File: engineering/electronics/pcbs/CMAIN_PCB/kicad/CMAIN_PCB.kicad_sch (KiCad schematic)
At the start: 79 parts, among them IC1 TSYS01, J1 RPI_5_WITH_SSQ-120-01-F-D, J10 1778719, J11 M9N-G4-3100, J12 B04B-JWPF-SK-R, J13 B04B-JWPF-SK-R, J14 XT30PW-F, J15 SM04B-GHS-TB_LF__SN_, J16 1778719, J17 SM03B-GHS-TB(LF)(SN), J19 1778719, J2 1778719, J21 1778719, J23 B04B-JWPF-SK-R, J24 1778719, J27 B04B-JWPF-SK-R, J29 B06B-JWPF-SK-R, J3 AXK6S00547YG, J30 B06B-JWPF-SK-R, J31 B06B-JWPF-SK-R, J32 B04B-JWPF-SK-R, J35 SM04B-GHS-TB_LF__SN_, J36 SM05B-GHS-TB_LF__SN_, J37 B04B-JWPF-SK-R, J38 B04B-JWPF-SK-R, J39 B04B-JWPF-SK-R, J4 AXK6S00547YG, J40 B04B-JWPF-SK-R, J41 SM06B-GHS-TB_LF__SN_, J43 B04B-JWPF-SK-R, J45 B04B-JWPF-SK-R, J46 B04B-JWPF-SK-R, J48 B04B-JWPF-SK-R, J49 B04B-JWPF-SK-R, J5 SM04B-GHS-TB_LF__SN_, J50 1778719, J52 B04B-JWPF-SK-R, J53 B04B-JWPF-SK-R, J55 B04B-JWPF-SK-R, J56 B04B-JWPF-SK-R, J57 B04B-JWPF-SK-R, J6 1778719, J7 SM04B-GHS-TB_LF__SN_, J8 B04B-JWPF-SK-R, J9 SM04B-GHS-TB_LF__SN_, U10 SMTSO25100CTJ, U11 SMTSO25100CTJ, U12 SMTSO25100CTJ, U3 SMTSOM380BTR, U6 SMTSOM380BTR, U7 SMTSOM380BTR, U8 SMTSOM380BTR, U9 SMTSO25100CTJ

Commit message: Resolve CMAIN ERC warnings
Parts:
- CN18, CN20, CN22, CN54: symbol EasyEDA_Lib_CMAIN:BM04B-GHS-TBT(LF)(SN) -> CMAIN_PCB:BM04B-GHS-TBT(LF)(SN)
- D5: symbol EasyEDA_Lib_CMAIN:USBLC6-2SC6 -> CMAIN_PCB:USBLC6-2SC6
- D8: symbol EasyEDA_Lib_CMAIN:SS14_C7420316 -> CMAIN_PCB:SS14_C7420316
- U19, U20, U21, U5: symbol EasyEDA_Lib_CMAIN:SMTSO3050CTJ -> CMAIN_PCB:SMTSO3050CTJ
- USB33: symbol EasyEDA_Lib_CMAIN:TYPEC-303-ACP16 -> CMAIN_PCB:TYPEC-303-ACP16
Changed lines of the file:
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@@
 	)
 	(symbol
-		(lib_id "EasyEDA_Lib_CMAIN:SMTSO3050CTJ")
+		(lib_id "CMAIN_PCB:SMTSO3050CTJ")
 		(at 137.16 216.662 0)
 		(unit 1)
@@
 	)
 	(symbol
-		(lib_id "EasyEDA_Lib_CMAIN:USBLC6-2SC6")
+		(lib_id "CMAIN_PCB:USBLC6-2SC6")
 		(at 485.648 325.628 0)
 		(unit 1)
@@
 	)
 	(symbol
-		(lib_id "EasyEDA_Lib_CMAIN:BM04B-GHS-TBT(LF)(SN)")
+		(lib_id "CMAIN_PCB:BM04B-GHS-TBT(LF)(SN)")
 		(at 285.75 151.13 0)
 		(unit 1)
@@
 	)
 	(symbol
-		(lib_id "EasyEDA_Lib_CMAIN:BM04B-GHS-TBT(LF)(SN)")
+		(lib_id "CMAIN_PCB:BM04B-GHS-TBT(LF)(SN)")
 		(at 265.43 158.75 0)
 		(unit 1)
@@
 	)
 	(symbol
-		(lib_id "EasyEDA_Lib_CMAIN:SMTSO3050CTJ")
+		(lib_id "CMAIN_PCB:SMTSO3050CTJ")
 		(at 137.16 233.172 0)
 		(unit 1)
@@
 	)
 	(symbol
-		(lib_id "EasyEDA_Lib_CMAIN:TYPEC-303-ACP16")
+		(lib_id "CMAIN_PCB:TYPEC-303-ACP16")
 		(at 425.958 325.628 180)
 		(unit 1)
@@
 	)
 	(symbol
-		(lib_id "EasyEDA_Lib_CMAIN:BM04B-GHS-TBT(LF)(SN)")
+		(lib_id "CMAIN_PCB:BM04B-GHS-TBT(LF)(SN)")
 		(at 306.07 156.21 0)
 		(unit 1)
@@
 	)
 	(symbol
-		(lib_id "EasyEDA_Lib_CMAIN:BM04B-GHS-TBT(LF)(SN)")
+		(lib_id "CMAIN_PCB:BM04B-GHS-TBT(LF)(SN)")
 		(at 242.57 153.67 0)
 		(unit 1)
@@
 	)
 	(symbol
-		(lib_id "EasyEDA_Lib_CMAIN:SS14_C7420316")
+		(lib_id "CMAIN_PCB:SS14_C7420316")
 		(at 453.898 309.118 0)
 		(unit 1)
@@
 	)
 	(symbol
-		(lib_id "EasyEDA_Lib_CMAIN:SMTSO3050CTJ")
+		(lib_id "CMAIN_PCB:SMTSO3050CTJ")
 		(at 137.16 222.25 0)
 		(unit 1)
@@
 	)
 	(symbol
-		(lib_id "EasyEDA_Lib_CMAIN:SMTSO3050CTJ")
+		(lib_id "CMAIN_PCB:SMTSO3050CTJ")
 		(at 137.16 227.584 0)
 		(unit 1)

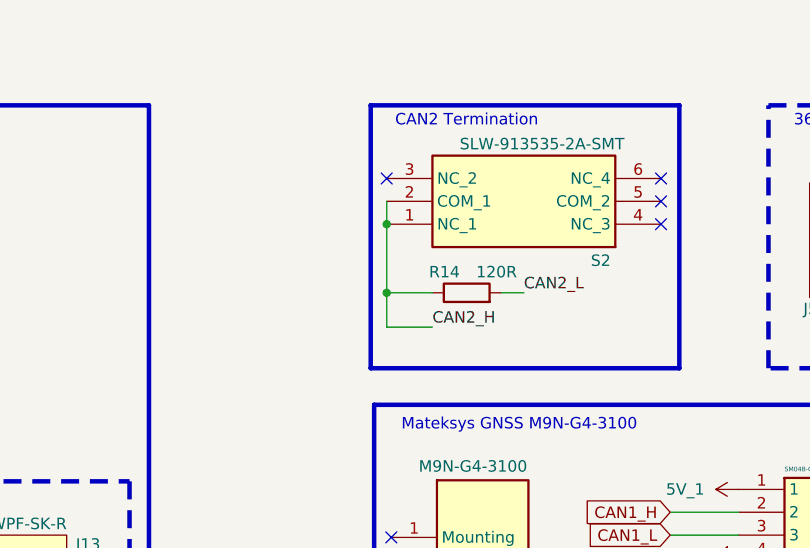
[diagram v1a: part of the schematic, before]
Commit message: Update CMAIN PCB routing from latest archive
Import Julius's latest CMAIN KiCad update, excluding local .history and backup archives. Remap undefined Rescue footprint graphics to F.Fab so KiCad CLI can load the board, and add KiCad ERC/DRC reports.
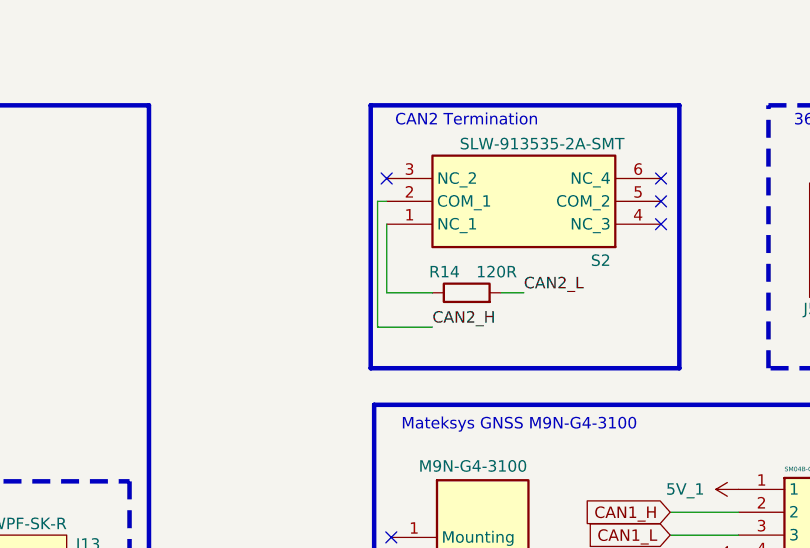
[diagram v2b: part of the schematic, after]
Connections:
- net CAN2_H: no longer R14.1, S2.1 (NC_1)
- new net: R14.1, S2.1 (NC_1)
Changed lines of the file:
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@@
-	)
-	(junction
-		(at 407.416 46.228)
-		(diameter 0)
-		(color 0 0 0 0)
 	)
 	(junction
@@
 	)
 	(junction
-		(at 407.416 38.608)
-		(diameter 0)
-		(color 0 0 0 0)
-	)
-	(junction
 		(at 106.426 223.012)
 		(diameter 0)
@@
 	(wire
 		(pts
+			(xy 406.4 36.068) (xy 407.416 36.068)
+		)
+		(stroke
+			(width 0)
+			(type default)
+		)
+	)
+	(wire
+		(pts
 			(xy 255.143 321.818) (xy 255.143 316.738)
 		)
@@
 	(wire
 		(pts
+			(xy 407.416 38.608) (xy 407.416 46.228)
+		)
+		(stroke
+			(width 0)
+			(type default)
+		)
+	)
+	(wire
+		(pts
 			(xy 255.016 286.004) (xy 261.366 286.004)
 		)
@@
 	(wire
 		(pts
+			(xy 406.4 50.038) (xy 412.496 50.038)
+		)
+		(stroke
+			(width 0)
+			(type default)
+		)
+	)
+	(wire
+		(pts
 			(xy 433.578 314.198) (xy 441.96 314.198)
 		)
@@
 	(wire
 		(pts
+			(xy 406.4 50.038) (xy 406.4 36.068)
+		)
+		(stroke
+			(width 0)
+			(type default)
+		)
+	)
+	(wire
+		(pts
 			(xy 460.248 318.008) (xy 469.138 318.008)
 		)
@@
 	(wire
 		(pts
-			(xy 407.416 50.038) (xy 412.496 50.038)
-		)
-		(stroke
-			(width 0)
-			(type default)
-		)
-	)
-	(wire
-		(pts
 			(xy 424.18 171.196) (xy 426.72 171.196)
 		)
@@
 	(wire
 		(pts
-			(xy 407.416 36.068) (xy 407.416 38.608)
-		)
-		(stroke
-			(width 0)
-			(type default)
-		)
-	)
-	(wire
-		(pts
 			(xy 327.914 113.538) (xy 335.534 113.538)
 		)
@@
 	(wire
 		(pts
-			(xy 407.416 46.228) (xy 407.416 50.038)
-		)
-		(stroke
-			(width 0)
-			(type default)
-		)
-	)
-	(wire
-		(pts
 			(xy 359.156 80.772) (xy 359.156 83.312)
 		)
@@
 		)
 		(stroke
-			(width 0)
-			(type default)
-		)
-	)
-	(wire
-		(pts
-			(xy 407.416 38.608) (xy 407.416 46.228)
-		)
-		(stroke

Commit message: Clean up CMAIN part value fields
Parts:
- C1: value 100nF -> 100nF 50V; footprint CMAIN_PCB:fp_71505040a9 -> Capacitor_SMD:C_0805_2012Metric_Pad1.18x1.45mm_HandSolder
- CN18, CN20, CN22, CN54: value (none) -> BM04B-GHS-TBT(LF)(SN)
- D5: value (none) -> USBLC6-2SC6
- D8: value (none) -> SS14
- J11: now not fitted
- R10, R11: value 10k -> 10k 150V; footprint CMAIN_PCB:fp_9fb50b8536 -> Resistor_SMD:R_0805_2012Metric_Pad1.20x1.40mm_HandSolder
- R12, R13: value 5K1 -> 5K1 150V; footprint CMAIN_PCB:fp_9fb50b8536 -> Resistor_SMD:R_0805_2012Metric_Pad1.20x1.40mm_HandSolder
- R14: value 120R -> 120R 150V; footprint CMAIN_PCB:fp_9fb50b8536 -> Resistor_SMD:R_0805_2012Metric_Pad1.20x1.40mm_HandSolder
- R2, R4, R5, R8: value 100k -> 100k 150V; footprint CMAIN_PCB:fp_9fb50b8536 -> Resistor_SMD:R_0805_2012Metric_Pad1.20x1.40mm_HandSolder
- U19, U20, U21, U5: value (none) -> SMTSO3050CTJ
- USB33: value (none) -> TYPEC-303-ACP16
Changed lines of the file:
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@@
 			)
 		)
-		(property "Value" ""
+		(property "Value" "SMTSO3050CTJ"
 			(at 137.16 216.662 0)
 			(show_name no)
@@
 			)
 		)
-		(property "Value" "100nF"
+		(property "Value" "100nF 50V"
 			(at 448.31 136.906 0)
 			(show_name no)
@@
 			)
 		)
-		(property "Footprint" "CMAIN_PCB:fp_71505040a9"
+		(property "Footprint" "Capacitor_SMD:C_0805_2012Metric_Pad1.18x1.45mm_HandSolder"
 			(at 448.31 143.256 0)
 			(hide yes)
@@
 			)
 		)
-		(property "Value" "120R"
+		(property "Value" "120R 150V"
 			(at 421.894 43.18 90)
 			(show_name no)
@@
 			)
 		)
-		(property "Footprint" "CMAIN_PCB:fp_9fb50b8536"
+		(property "Footprint" "Resistor_SMD:R_0805_2012Metric_Pad1.20x1.40mm_HandSolder"
 			(at 416.306 47.498 90)
 			(hide yes)
@@
 			)
 		)
-		(property "Value" ""
+		(property "Value" "USBLC6-2SC6"
 			(at 485.648 325.628 0)
 			(show_name no)
@@
 			)
 		)
-		(property "Value" ""
+		(property "Value" "BM04B-GHS-TBT(LF)(SN)"
 			(at 285.75 151.13 0)
 			(show_name no)
@@
 			)
 		)
-		(property "Value" "10k"
+		(property "Value" "10k 150V"
 			(at 429.26 171.196 90)
 			(show_name no)
@@
 			)
 		)
-		(property "Footprint" "CMAIN_PCB:fp_9fb50b8536"
+		(property "Footprint" "Resistor_SMD:R_0805_2012Metric_Pad1.20x1.40mm_HandSolder"
 			(at 430.53 169.926 90)
 			(hide yes)
@@
 			)
 		)
-		(property "Value" ""
+		(property "Value" "BM04B-GHS-TBT(LF)(SN)"
 			(at 265.43 158.75 0)
 			(show_name no)
@@
 		(on_board yes)
 		(in_pos_files yes)
-		(dnp no)
+		(dnp yes)
 		(property "Reference" "J11"
 			(at 413.004 81.026 0)
@@
 			)
 		)
-		(property "Value" ""
+		(property "Value" "SMTSO3050CTJ"
 			(at 137.16 233.172 0)
 			(show_name no)
@@
 			)
 		)
-		(property "Value" "100k"
+		(property "Value" "100k 150V"
 			(at 461.01 166.116 90)
 			(show_name no)
@@
 			)
 		)
-		(property "Footprint" "CMAIN_PCB:fp_9fb50b8536"
+		(property "Footprint" "Resistor_SMD:R_0805_2012Metric_Pad1.20x1.40mm_HandSolder"
 			(at 458.47 167.386 90)
 			(hide yes)
@@
 			)
 		)
-		(property "Value" "5K1"
+		(property "Value" "5K1 150V"
 			(at 446.532 345.694 90)
 			(show_name no)
@@
 			)
 		)
-		(property "Footprint" "CMAIN_PCB:fp_9fb50b8536"
+		(property "Footprint" "Resistor_SMD:R_0805_2012Metric_Pad1.20x1.40mm_HandSolder"
 			(at 446.532 345.694 0)
 			(hide yes)
@@
 			)
 		)
-		(property "Value" ""
+		(property "Value" "TYPEC-303-ACP16"
 			(at 425.958 325.628 0)
 			(show_name no)
@@
 			)
 		)
-		(property "Value" ""
+		(property "Value" "BM04B-GHS-TBT(LF)(SN)"
 			(at 306.07 156.21 0)
 			(show_name no)
@@
 			)
 		)
-		(property "Value" ""
+		(property "Value" "BM04B-GHS-TBT(LF)(SN)"
 			(at 242.57 153.67 0)
 			(show_name no)
@@
 			)
 		)
-		(property "Value" ""
+		(property "Value" "SS14"
 			(at 453.898 309.118 0)
 			(show_name no)
@@
 			)
 		)
-		(property "Value" "5K1"
+		(property "Value" "5K1 150V"
 			(at 456.438 340.868 90)
 			(show_name no)
@@
 			)
 		)
-		(property "Footprint" "CMAIN_PCB:fp_9fb50b8536"
+		(property "Footprint" "Resistor_SMD:R_0805_2012Metric_Pad1.20x1.40mm_HandSolder"
 			(at 456.438 340.868 0)
 			(hide yes)
@@
 			)
 		)
-		(property "Value" "10k"
+		(property "Value" "10k 150V"
 			(at 430.53 173.736 90)
 			(show_name no)
@@
 			)
 		)
-		(property "Footprint" "CMAIN_PCB:fp_9fb50b8536"
+		(property "Footprint" "Resistor_SMD:R_0805_2012Metric_Pad1.20x1.40mm_HandSolder"
 			(at 431.8 172.466 90)
 			(hide yes)
@@
 			)
 		)
-		(property "Value" ""
+		(property "Value" "SMTSO3050CTJ"
 			(at 137.16 222.25 0)
 			(show_name no)
@@
 			)
 		)
-		(property "Value" "100k"
+		(property "Value" "100k 150V"
 			(at 434.34 134.366 90)
 			(show_name no)
@@
 			)
 		)
-		(property "Footprint" "CMAIN_PCB:fp_9fb50b8536"
+		(property "Footprint" "Resistor_SMD:R_0805_2012Metric_Pad1.20x1.40mm_HandSolder"
 			(at 435.61 136.906 90)
 			(hide yes)
@@
 			)
 		)
-		(property "Value" "100k"
+		(property "Value" "100k 150V"
 			(at 457.2 116.586 90)
 			(show_name no)
@@
 			)
 		)
-		(property "Footprint" "CMAIN_PCB:fp_9fb50b8536"
+		(property "Footprint" "Resistor_SMD:R_0805_2012Metric_Pad1.20x1.40mm_HandSolder"
 			(at 455.93 117.856 90)
 			(hide yes)
@@
 			)
 		)
-		(property "Value" "100k"
+		(property "Value" "100k 150V"
 			(at 438.15 134.366 90)
 			(show_name no)
@@
 			)
 		)
-		(property "Footprint" "CMAIN_PCB:fp_9fb50b8536"
+		(property "Footprint" "Resistor_SMD:R_0805_2012Metric_Pad1.20x1.40mm_HandSolder"
 			(at 439.42 136.906 90)
 			(hide yes)
@@
 			)
 		)
-		(property "Value" ""
+		(property "Value" "SMTSO3050CTJ"
 			(at 137.16 227.584 0)
 			(show_name no)

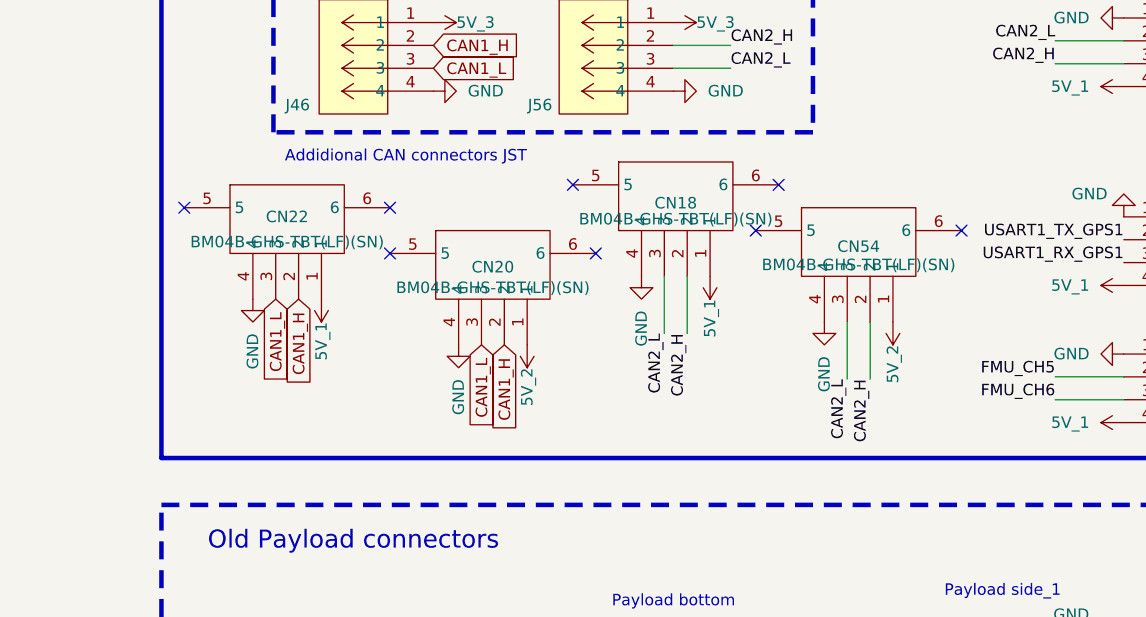
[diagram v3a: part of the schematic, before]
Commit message: fix(cmain): import KiCad updates with native libs
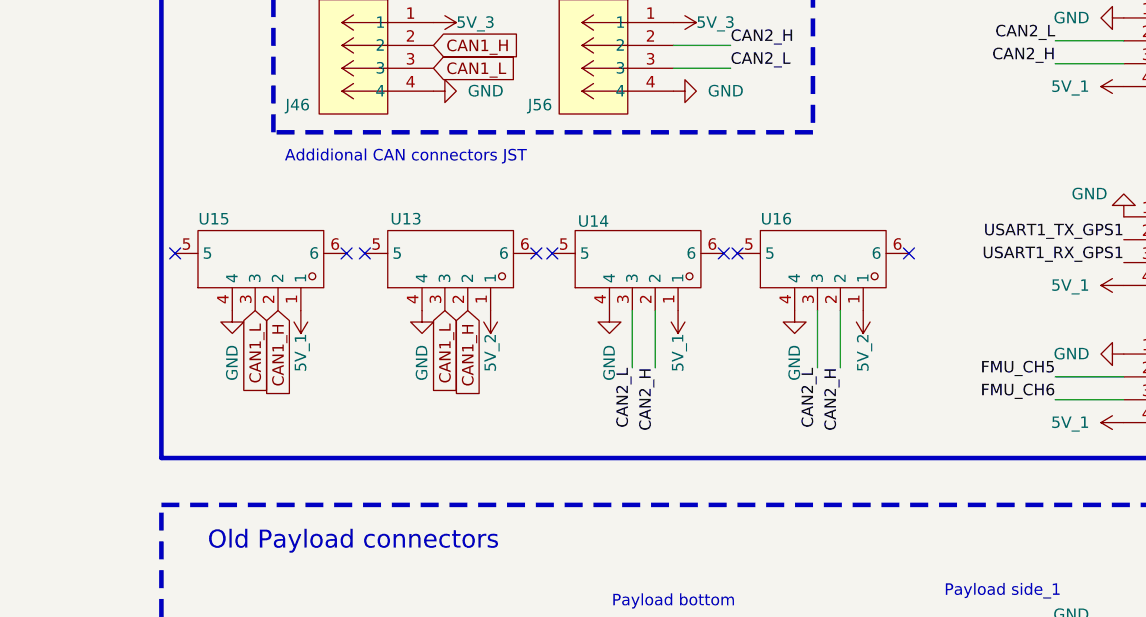
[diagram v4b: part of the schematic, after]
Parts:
- D5: footprint EasyEDA_Lib:SOT-23-6_L2.9-W1.6-P0.95-LS2.8-BL -> CMAIN_PCB:SOT-23-6_L2.9-W1.6-P0.95-LS2.8-BL
- U10, U11, U12, U9: footprint CMAIN_PCB:SMD_BD5.6-L5.6-W5.6-D4.1 -> CMAIN_PCB:SMD_SMTSO25100CTJ
- U13: renamed from CN20; value BM04B-GHS-TBT(LF)(SN) -> (none); footprint EasyEDA_Lib:fp_49628edcd6 -> CMAIN_PCB:WAFER-GH1.25-4PLB; symbol CMAIN_PCB:BM04B-GHS-TBT(LF)(SN) -> CMAIN_PCB:WAFER-GH1.25-4PLB; Manufacturer JST -> XUNPU(讯普); Manufacturer Part BM04B-GHS-TBT(LF)(SN) -> WAFER-GH1.25-4PLB; Supplier Part C161692 -> C3029370
- U14: renamed from CN18; value BM04B-GHS-TBT(LF)(SN) -> (none); footprint EasyEDA_Lib:fp_49628edcd6 -> CMAIN_PCB:WAFER-GH1.25-4PLB; symbol CMAIN_PCB:BM04B-GHS-TBT(LF)(SN) -> CMAIN_PCB:WAFER-GH1.25-4PLB; Manufacturer JST -> XUNPU(讯普); Manufacturer Part BM04B-GHS-TBT(LF)(SN) -> WAFER-GH1.25-4PLB; Supplier Part C161692 -> C3029370
- U15: renamed from CN22; value BM04B-GHS-TBT(LF)(SN) -> (none); footprint EasyEDA_Lib:fp_49628edcd6 -> CMAIN_PCB:WAFER-GH1.25-4PLB; symbol CMAIN_PCB:BM04B-GHS-TBT(LF)(SN) -> CMAIN_PCB:WAFER-GH1.25-4PLB; Manufacturer JST -> XUNPU(讯普); Manufacturer Part BM04B-GHS-TBT(LF)(SN) -> WAFER-GH1.25-4PLB; Supplier Part C161692 -> C3029370
- U16: renamed from CN54; value BM04B-GHS-TBT(LF)(SN) -> (none); footprint EasyEDA_Lib:fp_49628edcd6 -> CMAIN_PCB:WAFER-GH1.25-4PLB; symbol CMAIN_PCB:BM04B-GHS-TBT(LF)(SN) -> CMAIN_PCB:WAFER-GH1.25-4PLB; Manufacturer JST -> XUNPU(讯普); Manufacturer Part BM04B-GHS-TBT(LF)(SN) -> WAFER-GH1.25-4PLB; Supplier Part C161692 -> C3029370

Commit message: fix(cmain): integrate prototype ordering update
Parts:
- removed U10, U11, U12, U9: SMTSO25100CTJ, CMAIN_PCB:SMD_SMTSO25100CTJ, symbol Snapeda:SMTSO25100CTJ
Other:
- note removed: "Threaded standoffs for mounting the RPI"
- moved on the sheet: U19, U20, U21, U5
